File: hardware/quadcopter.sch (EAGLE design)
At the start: 27 parts, among them J1 AVR_SPI_PRG_6NS, J2 HEADER-4POS-2X2-0.1IN-FEMALE-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, U1 ATMEGA128RFA1, U2 IMU-LSM6DSOXTR-497-18367-1-ND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, Y1 CRYSTAL5X3

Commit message: fixing many eaglint errors, mostly disconnected nets
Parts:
- added B2: BATTERY-SCREW-TERMINAL-MINI-SMD, quadparts_prebuilt_2022:BATTERY-SCREW-TERMINAL-MINI-SMD
- added C14, C15: 1uF, quadparts_prebuilt_2022:CAPACITOR-NP_SMD-2012-0805_CERAMIC-1UF
- added C16: 47uF, quadparts_prebuilt_2022:CAPACITOR-POL_47UF-SMD-1206-TAJA
- added C9: 0.1uF, quadparts_prebuilt_2022:CAPACITOR-NP_SMD-2012-0805_CERAMIC-0.1UF
- added D10, D3, D4, D9: (no value), custom_v9:LED-RED-160-1178-1-ND
- added D5, D6, D7, D8: 360mV, quadparts_prebuilt_2022:DIODE-SCHOTTKY_-SMD-SOD123
- added J3: HEADER-10POSTH-254X10, quadparts_prebuilt_2022:HEADER-10POSTH-254X10
- added J4: HEADER-4POS-2X2-0.1IN-FEMALE-SMD-BOTTOM-ENTRY, quadparts_prebuilt_2022:HEADER-4POS-2X2-0.1IN-FEMALE-SMD-BOTTOM-ENTRY
- added Q3, Q4, Q5, Q6: MOSFET-FET-SI2302CDS-T1-E3CT-NDSI2302CDS-T1-E3CT-ND, custom_v9:MOSFET-FET-SI2302CDS-T1-E3CT-NDSI2302CDS-T1-E3CT-ND
- added R10, R11, R7, R8, R9: 10K, quadparts_prebuilt_2022:RESISTOR_SMD-2012-0805-10K
- added R13: 27K, quadparts_prebuilt_2022:RESISTOR_SMD-2012-0805-27K
- added R6: 604, quadparts_prebuilt_2022:RESISTOR_SMD-2012-0805-604
- added S1: POWER-SWITCH-MFS201N-9-Z-SMD-EDGE, quadparts_prebuilt_2022:POWER-SWITCH-MFS201N-9-Z-SMD-EDGE
- added U$1: 3V, quadparts_prebuilt_2022:TPS73633-DBVT3V
- added U$2: NETBRIDGE, custom:NETBRIDGE
- added U$3, U$4, U$5, U$6: MOTOR_PADS_GND-MOLEX-SMD, quadparts_prebuilt_2022:MOTOR_PADS_GND-MOLEX-SMD
- C11: value 0.1uF -> 47uF; device quadparts_prebuilt_2022:CAPACITOR-NP_SMD-2012-0805_CERAMIC-0.1UF -> quadparts_prebuilt_2022:CAPACITOR-POL_47UF-SMD-1206-TAJA
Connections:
- removed net 10: U1.PB0(SSN/PCINT0)
- removed net 2: U1.PE2(XCK0/AIN0)
- removed net 3: U1.PE3(OC3A/AIN1)
- removed net 4: U1.PE4(OC3B/INT4)
- removed net 5: U1.PE5(OC3C/INT5)
- removed net 6: U1.PE6(T3/INT6)
- removed net 7: U1.PE7(ICP3/INT7/CLKO)
- removed net 8: U1.PB5(OC1A/PCINT5)
- removed net 9: U1.PB4(OC2A/PCINT4)
- removed net A0: U1.PF0(ADC0)
- removed net A1: U1.PF1(ADC1)
- removed net A2: U1.PF2(ADC2/DIG2)
- removed net A3: U1.PF3(ADC3/DIG4)
- removed net A4: U1.PF4(ADC4/TCK)
- removed net A5: U1.PF5(ADC5/TMS)
- removed net A6: U1.PF6(ADC6/TDO)
- removed net A7: U1.PF7(ADC7/TDI)
- removed net AREF: U1.AREF
- removed net SD0/SA0: U2.SDO/SA0
- new net BATMEASURE: R13.1, R7.2, U1.PF1(ADC1)
- new net BAT_GND: C11.-, J3.8, Q4.S, Q5.S, Q6.S, R7.1, S1.OFF, U$1.GND, U$2.BAT_GND, U$3.GND, U$4.GND, U$5.GND, U$6.GND
- new net LED1: D3.A, U1.PG5(OC0B)
- new net LED2: D4.A, U1.PE3(OC3A/AIN1)
- new net LED3: D9.A, U1.PE4(OC3B/INT4)
- new net LED4: D10.A, U1.PE5(OC3C/INT5)
- new net N$12: C9.2, U2.VDD
- new net N$16: C11.+, Q3.S
- new net N$18: D5.A, Q3.D, U$3.V-
- new net N$19: D6.A, Q4.D, U$4.V-
- new net N$20: D7.A, Q5.D, U$5.V-
- new net N$21: D8.A, Q6.D, U$6.V-
- new net N$22: D10.C, D3.C, D4.C, D9.C, R6.2
- new net N$23: B2.N, C15.2, S1.C, U$1.EN
- new net PWM1: J3.3, Q3.G, R8.1, U1.PB4(OC2A/PCINT4)
- new net PWM2: J3.4, Q4.G, R9.1, U1.PB5(OC1A/PCINT5)
- new net PWM3: J3.5, Q5.G, R10.1, U1.PB6(OC1B/PCINT6)
- new net PWM4: J3.6, Q6.G, R11.1, U1.PB7(OC0A/OC1C/PCINT7)
- new net VBAT: B2.P, C15.1, D5.C, D6.C, D7.C, D8.C, J3.7, R13.2, S1.ON, U$1.IN, U$3.V+, U$4.V+, U$5.V+, U$6.V+
- new net VDDIO: R4.1, R5.1
- net 3V: now also C14.1, C16.+, J3.9, J4.2, U$1.OUT; no longer C10.2, C11.1, R4.2, R5.2, U2.VDD, U2.VDDIO
- net GND: now also C10.2, C14.2, C16.-, C9.1, J3.10, J4.1, R10.2, R11.2, R6.1, R8.2, R9.2, U$2.GND; no longer C10.1, C11.2
- net N$13: now also C10.1, U2.VDDIO; no longer R4.1
- net SCL: now also J3.1, J4.4, R5.2, U1.PD0(SCL/INT0)
- net SDA: now also J3.2, J4.3, R4.2, U1.PD1(SDA/INT1); no longer R5.1
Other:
- moved on the sheet: C10, R4, R5

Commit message: see what new issues we have
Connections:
- new net N$17: C15.2, U$1.EN
- net N$23: no longer C15.2, U$1.EN
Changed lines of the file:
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@@
 <pinref part="J3" gate="G$1" pin="8"/>
 <wire x1="91.44" y1="50.8" x2="96.52" y2="50.8" width="0.1524" layer="91"/>
-<label x="104.14" y="50.8" size="1.778" layer="95" xref="yes"/>
+<label x="96.52" y="50.8" size="1.778" layer="95" xref="yes"/>
 </segment>
 <segment>
@@
 <pinref part="U1" gate="G$1" pin="PB5(OC1A/PCINT5)"/>
 <wire x1="-177.8" y1="68.58" x2="-182.88" y2="68.58" width="0.1524" layer="91"/>
-<label x="-182.88" y="68.58" size="1.778" layer="95" rot="R180" xref="yes"/>
+<label x="-182.88" y="68.58" size="1.778" layer="95" rot="MR0" xref="yes"/>
 </segment>
 <segment>
 <pinref part="J3" gate="G$1" pin="4"/>
 <wire x1="91.44" y1="40.64" x2="104.14" y2="40.64" width="0.1524" layer="91"/>
-<label x="114.3" y="40.64" size="1.778" layer="95" xref="yes"/>
+<label x="104.14" y="40.64" size="1.778" layer="95" xref="yes"/>
 </segment>
 </net>
@@
 <pinref part="U1" gate="G$1" pin="PB7(OC0A/OC1C/PCINT7)"/>
 <wire x1="-177.8" y1="63.5" x2="-182.88" y2="63.5" width="0.1524" layer="91"/>
-<label x="-182.88" y="63.5" size="1.778" layer="95" rot="R180" xref="yes"/>
+<label x="-182.88" y="63.5" size="1.778" layer="95" rot="MR0" xref="yes"/>
 </segment>
 <segment>
 <pinref part="J3" gate="G$1" pin="6"/>
 <wire x1="91.44" y1="45.72" x2="104.14" y2="45.72" width="0.1524" layer="91"/>
-<label x="114.3" y="45.72" size="1.778" layer="95" xref="yes"/>
+<label x="104.14" y="45.72" size="1.778" layer="95" xref="yes"/>
 </segment>
 </net>
@@
 <net name="N$23" class="0">
 <segment>
+<pinref part="S1" gate="G$1" pin="C"/>
+<pinref part="B2" gate="G$1" pin="N"/>
+<wire x1="0" y1="-55.88" x2="-7.62" y2="-55.88" width="0.1524" layer="91"/>
+<wire x1="0" y1="-40.64" x2="0" y2="-55.88" width="0.1524" layer="91"/>
+</segment>
+</net>
+<net name="N$17" class="0">
+<segment>
+<pinref part="C15" gate="G$1" pin="2"/>
+<wire x1="15.24" y1="-50.8" x2="15.24" y2="-55.88" width="0.1524" layer="91"/>
 <pinref part="U$1" gate="G$1" pin="EN"/>
 <wire x1="22.86" y1="-55.88" x2="15.24" y2="-55.88" width="0.1524" layer="91"/>
-<pinref part="S1" gate="G$1" pin="C"/>
-<pinref part="B2" gate="G$1" pin="N"/>
-<wire x1="15.24" y1="-55.88" x2="0" y2="-55.88" width="0.1524" layer="91"/>
-<wire x1="0" y1="-55.88" x2="-7.62" y2="-55.88" width="0.1524" layer="91"/>
-<wire x1="0" y1="-40.64" x2="0" y2="-55.88" width="0.1524" layer="91"/>
-<junction x="0" y="-55.88"/>
-<pinref part="C15" gate="G$1" pin="2"/>
-<wire x1="15.24" y1="-50.8" x2="15.24" y2="-55.88" width="0.1524" layer="91"/>
-<junction x="15.24" y="-55.88"/>
-</segment>
-</net>
+</segment>
+</net>

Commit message: a few less errors
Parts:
- renumbered U$1 to VOLTAGE_REGULATOR, U$3 to MOTOR_PAD_1, U$4 to MOTOR_PAD_2, U$5 to MOTOR_PAD_3, U$6 to MOTOR_PAD_4
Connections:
- removed net N$14: C12.2
- net RESET: now also C12.2

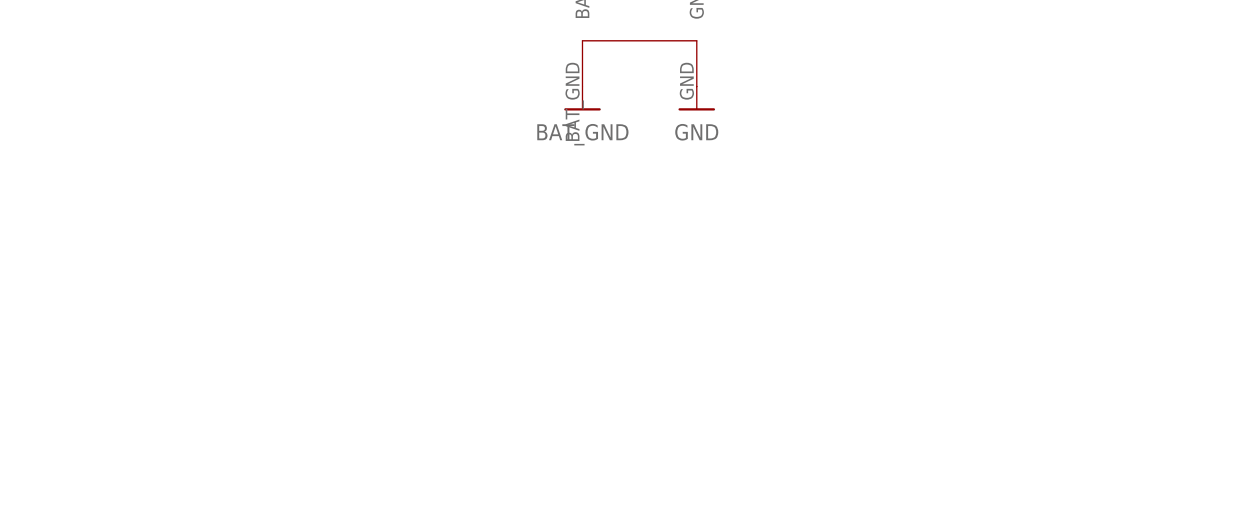
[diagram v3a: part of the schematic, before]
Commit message: fixing voltage regulator/switch
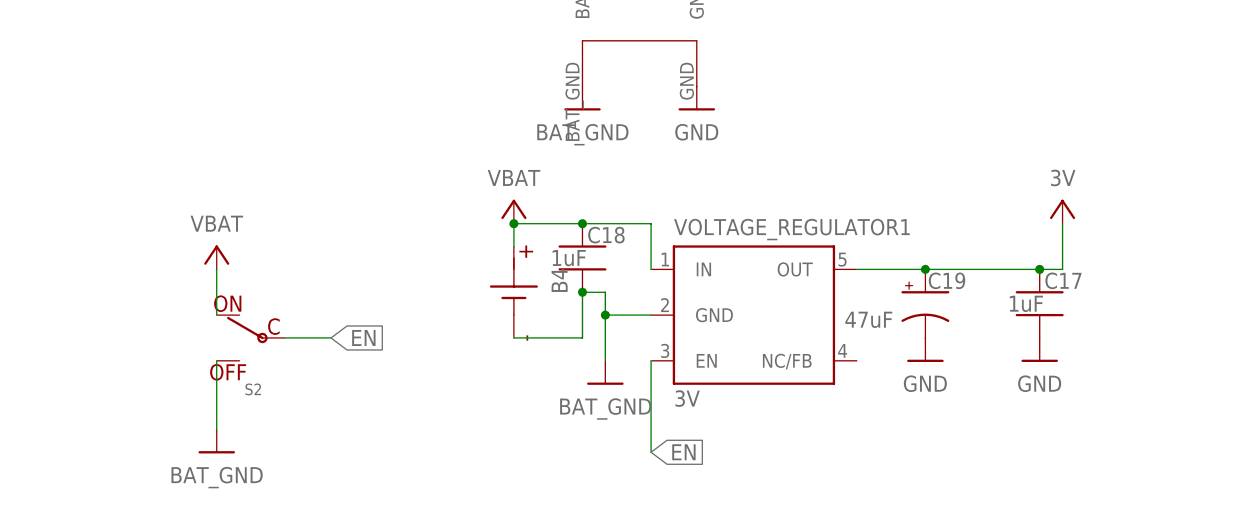
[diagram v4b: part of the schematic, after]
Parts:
- added B4: BATTERY-SCREW-TERMINAL-MINI-SMD, quadparts_prebuilt_2022:BATTERY-SCREW-TERMINAL-MINI-SMD
- added C17, C18: 1uF, quadparts_prebuilt_2022:CAPACITOR-NP_SMD-2012-0805_CERAMIC-1UF
- added C19: 47uF, quadparts_prebuilt_2022:CAPACITOR-POL_47UF-SMD-1206-TAJA
- added S2: POWER-SWITCH-MFS201N-9-Z-SMD-EDGE, quadparts_prebuilt_2022:POWER-SWITCH-MFS201N-9-Z-SMD-EDGE
- added VOLTAGE_REGULATOR1: 3V, quadparts_prebuilt_2022:TPS73633-DBVT3V
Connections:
- new net EN: S2.C, VOLTAGE_REGULATOR1.EN
- net 3V: now also C17.1, C19.+, VOLTAGE_REGULATOR1.OUT
- net BAT_GND: now also B4.N, C18.2, S2.OFF, VOLTAGE_REGULATOR1.GND
- net GND: now also C17.2, C19.-
- net VBAT: now also B4.P, C18.1, S2.ON, VOLTAGE_REGULATOR1.IN
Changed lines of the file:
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@@
 <part name="GND17" library="quadparts_prebuilt_2022" deviceset="GND" device=""/>
 <part name="GND20" library="quadparts_prebuilt_2022" deviceset="BAT_GND" device=""/>
+<part name="VOLTAGE_REGULATOR1" library="quadparts_prebuilt_2022" deviceset="TPS73633-DBVT" device="3V" value="3V"/>
+<part name="C17" library="quadparts_prebuilt_2022" deviceset="CAPACITOR-NP_" device="SMD-2012-0805_CERAMIC-1UF" value="1uF"/>
+<part name="C18" library="quadparts_prebuilt_2022" deviceset="CAPACITOR-NP_" device="SMD-2012-0805_CERAMIC-1UF" value="1uF"/>
+<part name="GND38" library="quadparts_prebuilt_2022" deviceset="GND" device=""/>
+<part name="C19" library="quadparts_prebuilt_2022" deviceset="CAPACITOR-POL_" device="47UF-SMD-1206-TAJA" package3d_urn="urn:adsk.eagle:package:11793387/1" value="47uF"/>
+<part name="GND39" library="quadparts_prebuilt_2022" deviceset="BAT_GND" device=""/>
+<part name="B4" library="quadparts_prebuilt_2022" deviceset="BATTERY" device="-SCREW-TERMINAL-MINI-SMD"/>
+<part name="P+17" library="quadparts_prebuilt_2022" deviceset="VBAT" device=""/>
+<part name="S2" library="quadparts_prebuilt_2022" deviceset="POWER-SWITCH-MFS201N-9-Z" device="-SMD-EDGE"/>
+<part name="P+18" library="quadparts_prebuilt_2022" deviceset="VBAT" device=""/>
+<part name="GND42" library="quadparts_prebuilt_2022" deviceset="BAT_GND" device=""/>
+<part name="GND43" library="quadparts_prebuilt_2022" deviceset="GND" device=""/>
+<part name="P+19" library="quadparts_prebuilt_2022" deviceset="3V" device=""/>
 </parts>
 <sheets>
@@
 <attribute name="VALUE" x="30.48" y="-86.36" size="1.778" layer="96" align="center"/>
 </instance>
+<instance part="VOLTAGE_REGULATOR1" gate="G$1" x="40.64" y="-114.3" smashed="yes">
+<attribute name="VALUE" x="40.64" y="-116.84" size="1.778" layer="96"/>
+<attribute name="NAME" x="40.64" y="-97.79" size="1.778" layer="95"/>
+</instance>
+<instance part="C17" gate="G$1" x="81.28" y="-104.14" smashed="yes">
+<attribute name="VALUE" x="77.724" y="-106.299" size="1.778" layer="96"/>
+<attribute name="NAME" x="81.788" y="-103.759" size="1.778" layer="95"/>
+</instance>
+<instance part="C18" gate="G$1" x="30.48" y="-99.06" smashed="yes">
+<attribute name="VALUE" x="26.924" y="-101.219" size="1.778" layer="96"/>
+<attribute name="NAME" x="30.988" y="-98.679" size="1.778" layer="95"/>
+</instance>
+<instance part="GND38" gate="1" x="81.28" y="-111.76" smashed="yes">
+<attribute name="VALUE" x="81.28" y="-114.3" size="1.778" layer="96" align="center"/>
+</instance>
+<instance part="C19" gate="G$1" x="68.58" y="-104.14" smashed="yes">
+<attribute name="VALUE" x="65.024" y="-106.299" size="1.778" layer="96" rot="R180"/>
+<attribute name="NAME" x="68.834" y="-103.759" size="1.778" layer="95"/>
+</instance>
+<instance part="GND39" gate="1" x="33.02" y="-114.3" smashed="yes">
+<attribute name="VALUE" x="33.02" y="-116.84" size="1.778" layer="96" align="center"/>
+</instance>
+<instance part="B4" gate="G$1" x="22.86" y="-104.14" smashed="yes" rot="R270">
+<attribute name="NAME" x="27.94" y="-102.87" size="1.778" layer="95" font="vector" rot="R270" align="center"/>
+</instance>
+<instance part="P+17" gate="VCC" x="22.86" y="-93.98" smashed="yes">
+<attribute name="VALUE" x="22.86" y="-91.44" size="1.778" layer="96" rot="R180" align="center"/>
+</instance>
+<instance part="S2" gate="G$1" x="-7.62" y="-109.22" smashed="yes" rot="MR0">
+<attribute name="NAME" x="-5.08" y="-115.57" size="1.27" layer="95" rot="MR0"/>
+</instance>
+<instance part="P+18" gate="VCC" x="-10.16" y="-99.06" smashed="yes">
+<attribute name="VALUE" x="-10.16" y="-96.52" size="1.778" layer="96" rot="R180" align="center"/>
+</instance>
+<instance part="GND42" gate="1" x="-10.16" y="-121.92" smashed="yes">
+<attribute name="VALUE" x="-10.16" y="-124.46" size="1.778" layer="96" align="center"/>
+</instance>
+<instance part="GND43" gate="1" x="68.58" y="-111.76" smashed="yes">
+<attribute name="VALUE" x="68.58" y="-114.3" size="1.778" layer="96" align="center"/>
+</instance>
+<instance part="P+19" gate="G$1" x="83.82" y="-93.98" smashed="yes">
+<attribute name="VALUE" x="83.82" y="-91.44" size="1.778" layer="96" rot="R180" align="center"/>
+</instance>
 </instances>
 <busses>
@@
 <pinref part="U$2" gate="G$1" pin="GND"/>
 <pinref part="GND17" gate="1" pin="GND"/>
+</segment>
+<segment>
+<pinref part="C17" gate="G$1" pin="2"/>
+<pinref part="GND38" gate="1" pin="GND"/>
+</segment>
+<segment>
+<pinref part="C19" gate="G$1" pin="-"/>
+<pinref part="GND43" gate="1" pin="GND"/>
 </segment>
 </net>
@@
 <wire x1="53.34" y1="-45.72" x2="45.72" y2="-45.72" width="0.1524" layer="91"/>
 <junction x="53.34" y="-45.72"/>
+</segment>
+<segment>
+<pinref part="P+19" gate="G$1" pin="3V"/>
+<wire x1="83.82" y1="-96.52" x2="83.82" y2="-101.6" width="0.1524" layer="91"/>
+<wire x1="83.82" y1="-101.6" x2="81.28" y2="-101.6" width="0.1524" layer="91"/>
+<pinref part="VOLTAGE_REGULATOR1" gate="G$1" pin="OUT"/>
+<pinref part="C17" gate="G$1" pin="1"/>
+<wire x1="81.28" y1="-101.6" x2="68.58" y2="-101.6" width="0.1524" layer="91"/>
+<junction x="81.28" y="-101.6"/>
+<pinref part="C19" gate="G$1" pin="+"/>
+<wire x1="68.58" y1="-101.6" x2="60.96" y2="-101.6" width="0.1524" layer="91"/>
+<junction x="68.58" y="-101.6"/>
 </segment>
 </net>
@@
 <pinref part="R13" gate="G$1" pin="2"/>
 </segment>
+<segment>
+<pinref part="VOLTAGE_REGULATOR1" gate="G$1" pin="IN"/>
+<wire x1="38.1" y1="-101.6" x2="38.1" y2="-96.52" width="0.1524" layer="91"/>
+<wire x1="38.1" y1="-96.52" x2="30.48" y2="-96.52" width="0.1524" layer="91"/>
+<pinref part="P+17" gate="VCC" pin="VBAT"/>
+<wire x1="30.48" y1="-96.52" x2="22.86" y2="-96.52" width="0.1524" layer="91"/>
+<wire x1="22.86" y1="-96.52" x2="22.86" y2="-99.06" width="0.1524" layer="91"/>
+<pinref part="B4" gate="G$1" pin="P"/>
+<junction x="22.86" y="-96.52"/>
+<pinref part="C18" gate="G$1" pin="1"/>
+<junction x="30.48" y="-96.52"/>
+</segment>
+<segment>
+<pinref part="S2" gate="G$1" pin="ON"/>
+<pinref part="P+18" gate="VCC" pin="VBAT"/>
+<wire x1="-10.16" y1="-101.6" x2="-10.16" y2="-106.68" width="0.1524" layer="91"/>
+</segment>
 </net>
 <net name="BAT_GND" class="0">
@@
 <wire x1="121.92" y1="-40.64" x2="121.92" y2="-35.56" width="0.1524" layer="91"/>
 <pinref part="R7" gate="G$1" pin="1"/>
+</segment>
+<segment>
+<pinref part="GND39" gate="1" pin="BAT_GND"/>
+<wire x1="33.02" y1="-111.76" x2="33.02" y2="-106.68" width="0.1524" layer="91"/>
+<wire x1="33.02" y1="-106.68" x2="33.02" y2="-104.14" width="0.1524" layer="91"/>
+<wire x1="33.02" y1="-106.68" x2="38.1" y2="-106.68" width="0.1524" layer="91"/>
+<pinref part="VOLTAGE_REGULATOR1" gate="G$1" pin="GND"/>
+<wire x1="33.02" y1="-104.14" x2="30.48" y2="-104.14" width="0.1524" layer="91"/>
+<pinref part="C18" gate="G$1" pin="2"/>
+<wire x1="30.48" y1="-104.14" x2="30.48" y2="-109.22" width="0.1524" layer="91"/>
+<wire x1="30.48" y1="-109.22" x2="22.86" y2="-109.22" width="0.1524" layer="91"/>
+<pinref part="B4" gate="G$1" pin="N"/>
+<junction x="33.02" y="-106.68"/>
+<junction x="30.48" y="-104.14"/>
+</segment>
+<segment>
+<pinref part="S2" gate="G$1" pin="OFF"/>
+<pinref part="GND42" gate="1" pin="BAT_GND"/>
+<wire x1="-10.16" y1="-119.38" x2="-10.16" y2="-111.76" width="0.1524" layer="91"/>
 </segment>
 </net>
@@
 </segment>
 </net>
+<net name="EN" class="0">
+<segment>
+<pinref part="S2" gate="G$1" pin="C"/>
+<wire x1="-2.54" y1="-109.22" x2="2.54" y2="-109.22" width="0.1524" layer="91"/>
+<label x="2.54" y="-109.22" size="1.778" layer="95" xref="yes"/>
+</segment>
+<segment>
+<pinref part="VOLTAGE_REGULATOR1" gate="G$1" pin="EN"/>
+<wire x1="38.1" y1="-111.76" x2="38.1" y2="-121.92" width="0.1524" layer="91"/>
+<label x="38.1" y="-121.92" size="1.778" layer="95" xref="yes"/>
+</segment>
+</net>
